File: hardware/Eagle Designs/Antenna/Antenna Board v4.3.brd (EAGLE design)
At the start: 100 x 100 mm, 20 parts, among them J1 5037630291, J10 MCX-J-P-X-ST-TH1, J11 U.FL-R-SMT-1(01), J12 MCX-J-P-X-ST-TH1, J13 MCX-J-P-X-ST-TH1, J14 UJ2-MIBH-G-SMT-TR, J15 MOLEX_503763-0491MOLEX_503763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, J16 ARJM11C7-104-AB-EW2, J2 503763-0591, J3 MOLEX_503763-0491MOLEX_503763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

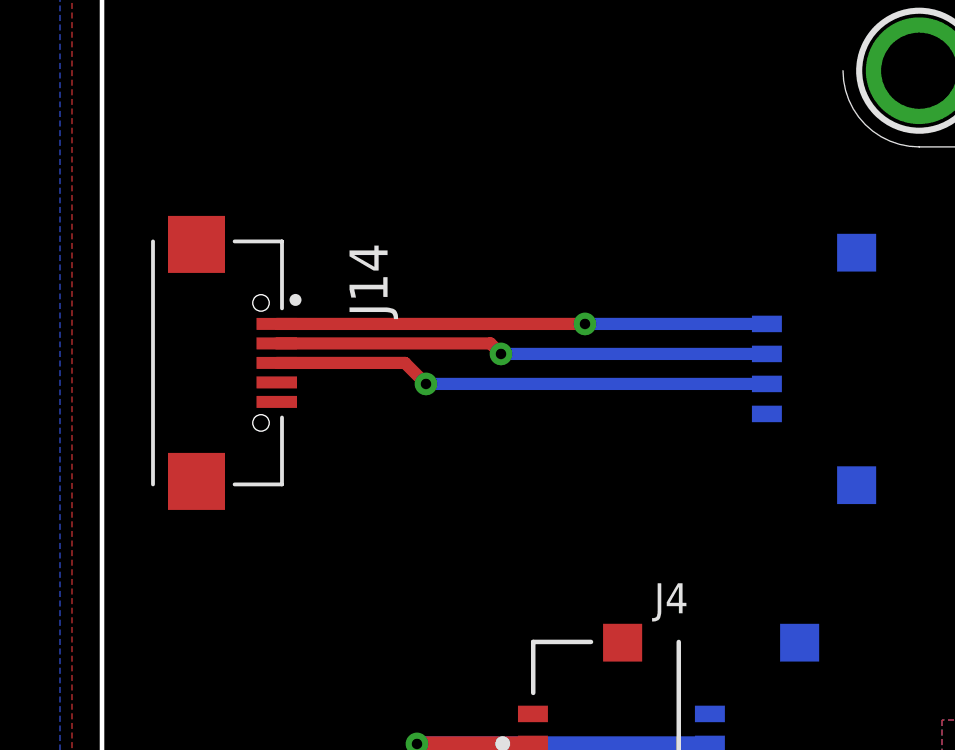
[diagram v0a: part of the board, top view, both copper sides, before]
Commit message: Antenna board edits
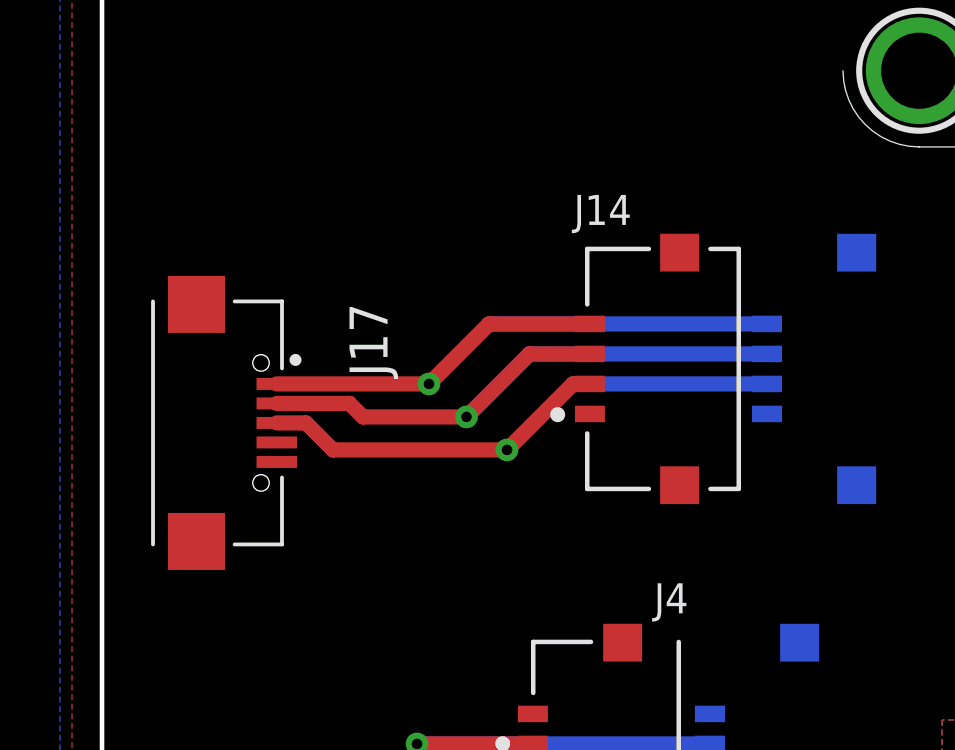
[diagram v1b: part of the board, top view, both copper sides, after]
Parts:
- added J17: UJ2-MIBH-G-SMT-TR, UJ2-MIBH-G-SMT-TR:CUI_UJ2-MIBH-G-SMT-TR
- J14: value UJ2-MIBH-G-SMT-TR -> MOLEX_503763-0491MOLEX_503763-0491_0_0; device UJ2-MIBH-G-SMT-TR:CUI_UJ2-MIBH-G-SMT-TR -> Molex - 503763-0491:MOLEX_503763-0491_0
- moved J14 15.6 mm to (18.7, 51.0)
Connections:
- net 5V: now also J14.4, J17.1; no longer J14.1
- net D+: now also J14.2, J17.3; no longer J14.3
- net D-: now also J14.3, J17.2; no longer J14.2
- net GND: now also J14.1, J14.6, J17.5, J17.S1, J17.S2; no longer J14.S1, J14.S2
- net ID: now also J17.4; no longer J14.4
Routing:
- net 5V: track 16.3 -> 23.4 mm
- net D-: track 16.5 -> 22.4 mm
- net D+: track 16.6 -> 21.3 mm
